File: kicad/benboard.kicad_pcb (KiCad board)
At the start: 4 copper layers, 140 x 88.4 mm, 58 parts, among them J1 USB_C_Receptacle_USB2.0, SW1 SW_Push, SW10 SW_Push, SW11 SW_Push, SW12 SW_Push, SW13 SW_Push, SW14 SW_Push, SW15 SW_Push, SW16 SW_Push, SW17 SW_Push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

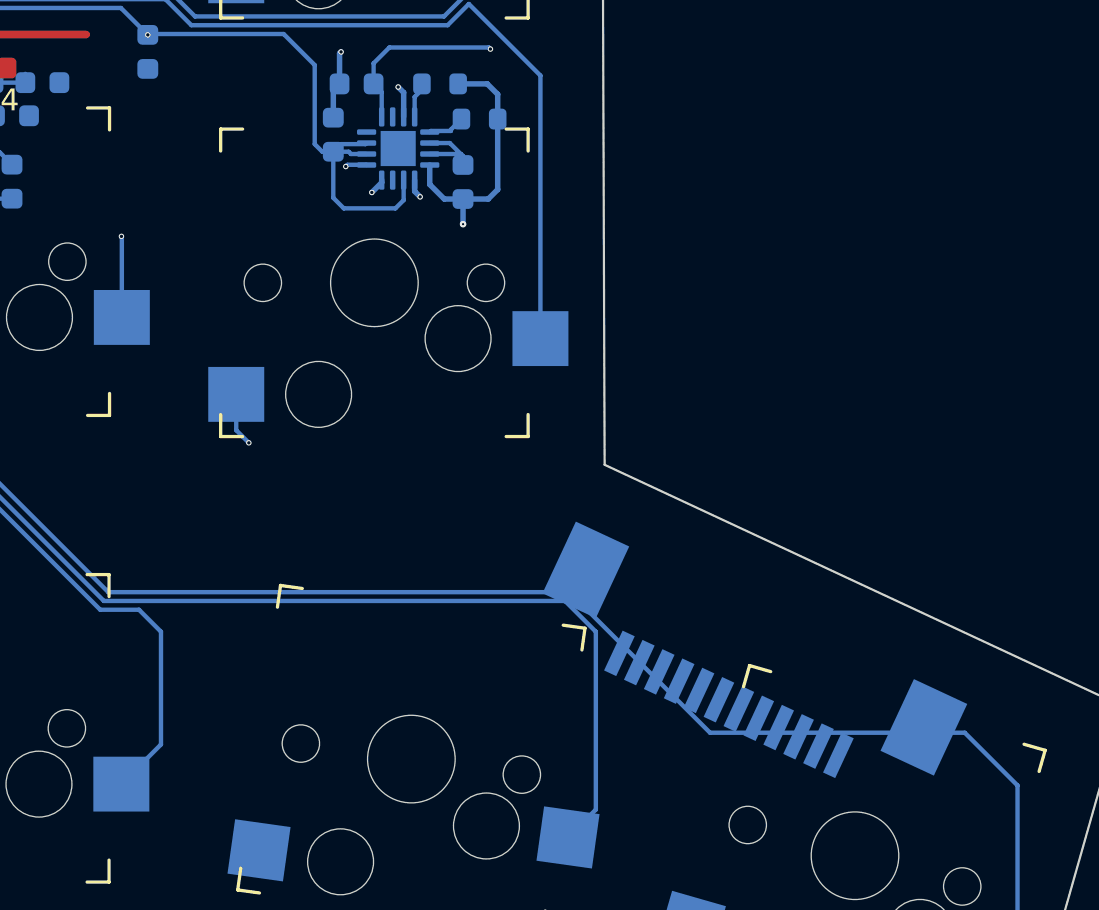
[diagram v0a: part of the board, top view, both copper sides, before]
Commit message: add vik and SWD
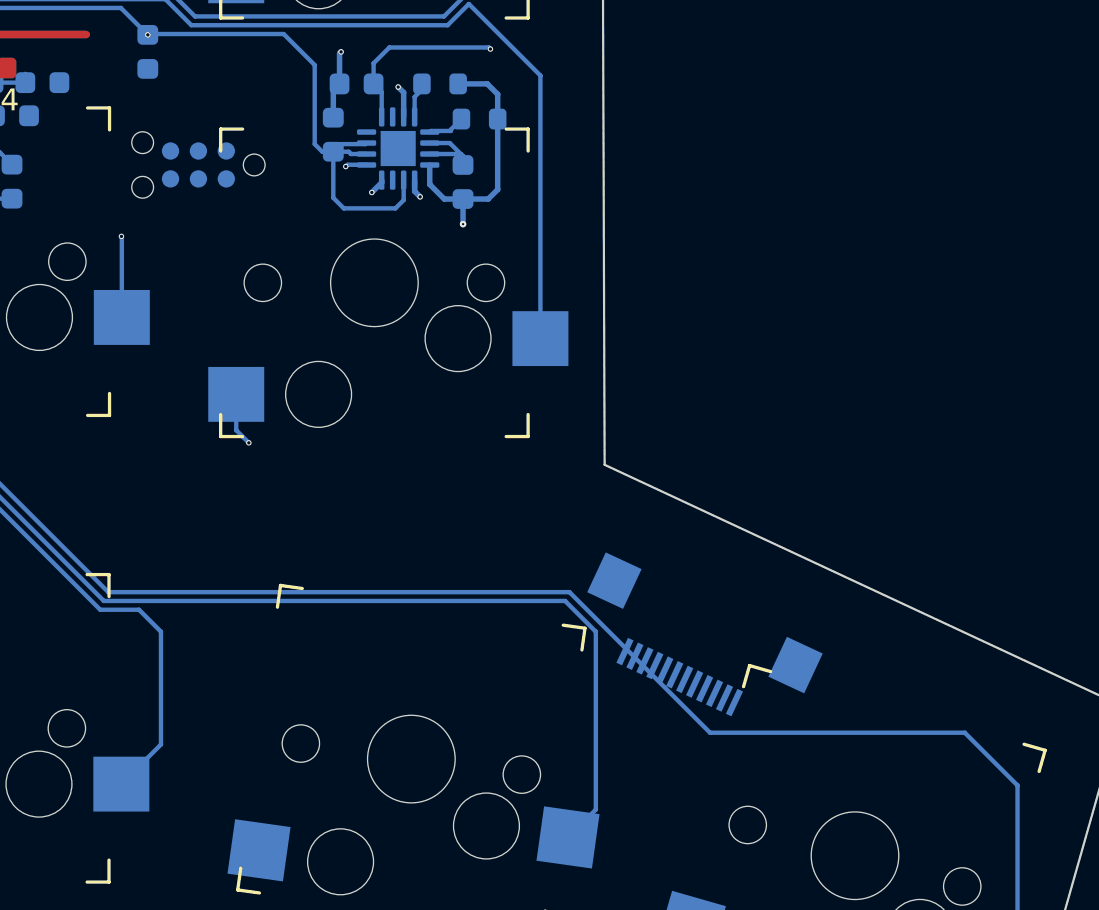
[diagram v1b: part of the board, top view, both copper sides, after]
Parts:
- removed C1: 4.7uF, Connector_FFC-FPC:TE_1-84953-2_1x12-1MP_P1.0mm_Horizontal
- added G***: LOGO, LOGO, B.Cu at (165.1, 108.4)
- added J2: ~, vik:vik-keyboard-connector-horizontal, B.Cu at (182.9, 109.2)
- added J3: Conn_ARM_SWD_TagConnect_TC2030-NL, Connector:Tag-Connect_TC2030-IDC-NL_2x03_P1.27mm_Vertical, B.Cu at (160.1, 87.7)
- added REF**: vik-logo-small, vik:vik-logo-small, B.Cu at (172.7, 108.4)
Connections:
- U1 pad A12: unconnected-(U1-AIN0/P0.02-PadA12) -> VIK_A0
- U1 pad A14: unconnected-(U1-P1.15-PadA14) -> SCLK
- U1 pad A16: unconnected-(U1-P1.13-PadA16) -> SPICS
- U1 pad A20: unconnected-(U1-P1.10-PadA20) -> SDA
- U1 pad B13: unconnected-(U1-AIN1/P0.03-PadB13) -> VIK_A1
- U1 pad B15: unconnected-(U1-P1.14-PadB15) -> MISO
- U1 pad B17: unconnected-(U1-P1.12-PadB17) -> MOSI
- U1 pad B19: unconnected-(U1-P1.11-PadB19) -> SCL
- U1 pad G1: unconnected-(U1-P0.26-PadG1) -> VIK_RGB

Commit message: routes for some stuff
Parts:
- added J4: Conn_01x02_Pin, Connector_JST:JST_EH_B2B-EH-A_1x02_P2.50mm_Vertical, F.Cu at (95.2, 71.8)
- added J5: Conn_Coaxial, Connector_Coaxial:SMA_Amphenol_132134-10_Vertical, F.Cu at (157.5, 83.6)
- added SW22: SW_Push, Button_Switch_SMD:SW_SPST_CK_KXT3, F.Cu at (156.6, 45.7)
- moved C20 74.8 mm to (99.0, 72.5)
- moved C19 67.5 mm to (101.3, 68.1)
- moved R4 67.5 mm to (108.0, 67.4)
- moved C18 67.5 mm to (102.4, 65.8)
- moved R5 67.5 mm to (106.2, 65.8)
- moved U2 67.5 mm to (104.3, 68.8)
- moved J3 21.4 mm to (153.6, 67.4), turned to 0 degrees
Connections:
- net ANTENNA renamed Net-(J5-Ext)
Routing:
- net SWDI: track 1.99 -> 34.4 mm
- net SWDC: track 3.22 -> 33.8 mm
- net VBUS: track 119.4 -> 149.2 mm
- net VBAT: track 3.72 -> 16.5 mm
- net GND: track 97.4 -> 86.4 mm, vias 25 -> 23
- net SW4: track 67.7 -> 59.7 mm
- net SW1: track 82.4 -> 80.5 mm
- net SW14: track 20.5 -> 19.7 mm, vias 1 -> 0
- net SW18: track 49.6 -> 49.0 mm
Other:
- board text added: "[-] SWD [-] RESET / POWER BUTTON [ ] ESD PROTECTION [-] BATTERY PADS [-] PROBE POINTS [-] ANT JUMPERS"
- board text removed: "- SWD - RESET / POWER BUTTON - ESD PROTECTION - BATTERY PADS - PROBE POINTS - ANT JUMPERS"

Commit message: wow
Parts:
- removed REF**: vik-logo-small, vik:vik-logo-small
- moved C2 55.5 mm to (103.0, 74.1)
- moved C16 9.42 mm to (157.6, 84.3)
- moved C17 9.42 mm to (161.0, 87.3)
- moved C3 9.42 mm to (162.3, 82.8)
- moved C4 9.42 mm to (161.0, 84.3)
- moved L1 9.42 mm to (156.3, 82.8)
- moved L2 9.42 mm to (159.3, 82.8)
- moved Y1 9.42 mm to (158.0, 86.9)
- moved C7 4.83 mm to (148.0, 83.8), turned to 0 degrees
- moved J5 1.42 mm to (158.9, 83.6)
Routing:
- net Net-(U1-XC2): track 9.84 -> 1.39 mm
- net Net-(U1-DEC4): track 22.4 -> 16.0 mm, vias 4 -> 1
- net SW20: track 67.6 -> 63.7 mm
- net Net-(U1-DCC): track 9.98 -> 6.28 mm, vias 2 -> 1
- net Net-(U1-XC1): track 4.82 -> 1.69 mm
- net SW15: track 24.6 -> 27.2 mm
- net GND: track 86.4 -> 84.0 mm
- net SW14: track 19.7 -> 21.2 mm
- net Net-(L1-Pad1): track 1.43 -> 0.00 mm
- net SWDC: track 33.8 -> 34.4 mm
- net SWDI: track 34.4 -> 35.1 mm
- net SW16: track 50.2 -> 50.9 mm
- net VDDH: track 89.0 -> 88.4 mm
- net Net-(U1-DEC3): track 3.60 -> 3.78 mm, vias 2 -> 0

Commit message: VIK Compatible
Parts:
- added C1: 4.7uF, Connector_FFC-FPC:TE_1-84953-2_1x12-1MP_P1.0mm_Horizontal, F.Cu at (10.5, 3.33)
- moved C17 6.38 mm to (154.8, 85.7)
- moved Y1 6.32 mm to (151.8, 85.5)
- moved C16 6.32 mm to (151.4, 82.8)
- moved C3 4.51 mm to (157.9, 83.7), turned to 90 degrees
- moved L1 3.25 mm to (156.4, 86.1), turned to 90 degrees
- moved L2 3.24 mm to (158.6, 86.0)
- moved C4 1.67 mm to (159.4, 83.7), turned to 90 degrees
- moved C7 0.62 mm to (147.5, 83.5)
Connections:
- U1 pad A10: unconnected-(U1-AIN5/P0.29-PadA10) -> SCLK
- U1 pad A14: SCLK -> MISO
- U1 pad A20: SDA -> MOSI
- U1 pad B15: MISO -> VIK_RGB
- U1 pad B17: MOSI -> SCL
- U1 pad B19: SCL -> SDA
- U1 pad G1: VIK_RGB -> unconnected-(U1-P0.26-PadG1)
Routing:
- net SCLK: track 0.00 -> 64.4 mm
- net MISO: track 0.00 -> 63.8 mm
- net SPICS: track 0.00 -> 62.9 mm
- net VIK_A1: track 0.00 -> 62.7 mm, vias 0 -> 2
- net VIK_A0: track 0.00 -> 60.9 mm, vias 0 -> 2
- net MOSI: track 0.00 -> 60.9 mm
- net VIK_RGB: track 0.00 -> 57.5 mm, vias 0 -> 2
- net SCL: track 0.00 -> 56.2 mm, vias 0 -> 2
- net SDA: track 0.00 -> 55.4 mm, vias 0 -> 2
- net VBUS: track 149.2 -> 187.6 mm
- net Net-(U1-DCC): track 6.28 -> 23.3 mm, vias 1 -> 2
- net Net-(U1-DEC4): track 16.0 -> 27.7 mm, vias 1 -> 3
- net Net-(U1-XC2): track 1.39 -> 12.9 mm
- net SW15: track 27.2 -> 37.0 mm
- net Net-(U1-XC1): track 1.69 -> 7.70 mm
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
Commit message: epic
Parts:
- removed C1: 4.7uF, Connector_FFC-FPC:TE_1-84953-2_1x12-1MP_P1.0mm_Horizontal
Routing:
- net GND: track 80.8 -> 88.2 mm
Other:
- board text added: "[x] SWD [x] VIK [-] RESET / POWER BUTTON [ ] ESD PROTECTION [ ] BETTER POWER CIRCUITRY (In1.Cu = 3v3) [x] BATTERY PADS [x] PROBE POINTS [-] ANT JUMPERS"
- board text removed: "[-] SWD [-] RESET / POWER BUTTON [ ] ESD PROTECTION [-] BATTERY PADS [-] PROBE POINTS [-] ANT JUMPERS"

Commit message: proper footprint
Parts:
- J5: footprint Connector_Coaxial:SMA_Amphenol_132134-10_Vertical -> Connector_Coaxial:U.FL_Hirose_U.FL-R-SMT-1_Vertical
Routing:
- net VDD_NRF: track 31.8 -> 32.4 mm
